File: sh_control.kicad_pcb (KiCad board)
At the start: 4 copper layers, 70 x 70 mm, 121 parts, among them IC1 SN65220DBVT, IC2 TUSB2046IBVF, IC3 ATMEGA328P-AU, IC4 FT232RL-REEL, IC5 LM317MDCY, J1 12401598E4#2A, J2 10129381-906001BLF, J3 10129381-906001BLF, Y1 6Mhz, Y2 16 MHz

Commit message: deleted all, beginning of eval board
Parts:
- removed C1, C14, C18, C19, C20, C21, C22, C23, C6: 10 uF, SamacSys_Parts:CAPC3216X180N
- removed C13: 1 uF, SamacSys_Parts:CAPC3216X210N
- removed C15, C17, C2, C4, C7: 0.1 uF, SamacSys_Parts:CAPC3216X88N
- removed C16, C24, C25, C26, C27: 100 uF, SamacSys_Parts:CAPPRD250W45D630H500
- removed C3, C5: 27 pF, SamacSys_Parts:CAPC3216X170N
- removed D1, D2, D3: FM4002-W, SamacSys_Parts:DIOM5025X231N
- removed DN_1, DN_2, DN_3, DN_4, DP_1, DP_2, DP_3, DP_4, GND1, GND2, GND_1, GND_2, GND_3, GND_4, LED_VCC_in1, LED_VCC_out1, VCC_1, VCC_2, VCC_3, VCC_4: TestPoint, TestPoint:TestPoint_Pad_2.0x2.0mm
- removed F1, F2: Fuse, SamacSys_Parts:FUSC4632X85N
- removed H1, H2, H3, H4: MountingHole, MountingHole:MountingHole_3.2mm_M3
- removed J1: 12401598E4#2A, usb c connector:AMPHENOL_12401598E4#2A
- removed J2, J3: 10129381-906001BLF, SamacSys_Parts:HDRV6W67P254_2X3_762X483X858P
- removed LED4, LED5, LED6, LED7, LED8, LED9: COM-13667, SamacSys_Parts:COM13667
- removed R1, R12, R15, R17, R18, R19, R2, R20, R7, R9: 22, SamacSys_Parts:RESC3116X70N
- removed R10, R13, R16, R21, R22, R23, R5, R8: 15K, SamacSys_Parts:RESC3216X75N
- removed R11, R4: 1K5, SamacSys_Parts:RESC2012X60N
- removed R14, R6: 4K7, SamacSys_Parts:RESC3116X65N
- removed R3: 10K, SamacSys_Parts:RESC3216X60N
- removed R31, R33: 390 R, SamacSys_Parts:RESC3216X60N
- removed R32: 240 R, SamacSys_Parts:RESC3216X75N
- removed Y1: 6Mhz, SamacSys_Parts:LFXTAL036567BULK
- added IC6: TLV76733DGNR, SamacSys_Parts:SOP65P490X110-9N, F.Cu at (90.3, 85.0)
- C10, C11, C12, C28, C29, C30, C31, C32, C33, C34, C35, C8, C9, IC3, IC4, LED1, LED2, LED3, PB0, PC5, PD2, PD3, PD7, R24, R25, R26, R27, R28, R29, R30, Y2: moved to F.Cu
- IC1: value SN65220DBVT -> TLV76733DGNR; footprint SamacSys_Parts:SOT95P280X145-6N -> SamacSys_Parts:SOP65P490X110-9N
- IC5: value LM317MDCY -> TPD2E2U06DCKR; footprint SamacSys_Parts:SOT230P700X180-4N -> SamacSys_Parts:SOT65P210X110-3N
- moved IC1 87.1 mm to (122.9, 58.9)
- moved PC5 86.8 mm to (128.6, 58.6)
- moved PD3 83.1 mm to (132.7, 58.6)
- moved PB0 81.9 mm to (121.3, 63.2)
- moved PD2 80.9 mm to (129.4, 62.6)
- moved PD7 72.7 mm to (125.3, 63.2)
- moved C35 71.8 mm to (112.1, 58.3), turned to 0 degrees
- moved C34 70.3 mm to (112.1, 61.7), turned to 0 degrees
- moved C29 70.2 mm to (106.4, 68.3), turned to 0 degrees
- moved C33 66.1 mm to (106.5, 65.0), turned to 0 degrees
- moved R30 66.0 mm to (106.6, 61.6), turned to 0 degrees
- moved C31 61.6 mm to (99.8, 69.8), turned to 0 degrees
- moved C30 60.3 mm to (99.2, 73.1), turned to 0 degrees
- moved C10 59.4 mm to (111.6, 68.3), turned to 0 degrees
- moved C12 59.2 mm to (111.9, 65.1)
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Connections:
- C10 pad 2: USB_GND -> GND
- C12 pad 1: USB_GND -> GND
- C28 pad 2: USB_GND -> GND
- C29 pad 2: USB_GND -> GND
- C30 pad 2: USB_GND -> GND
- C31 pad 2: USB_GND -> GND
- C32 pad 2: USB_GND -> GND
- C33 pad 2: USB_GND -> GND
- C34 pad 2: USB_GND -> GND
- C35 pad 2: USB_GND -> GND
- C8 pad 1: USB_GND -> GND
- C9 pad 1: USB_GND -> GND
- IC1 pad 2: USB_GND -> Net-(IC1-Pad2)
- IC1 pad 4: DN_hub -> Net-(IC1-Pad4)
- IC1 pad 5: USB_GND -> Net-(IC1-Pad5)
- IC1 pad 6: DP_hub -> Net-(IC1-Pad6)
- IC2 pad 14: Net-(IC2-Pad10) -> Net-(IC2-Pad14)
- IC2 pad 18: Net-(IC2-Pad10) -> Net-(IC2-Pad18)
- IC2 pad 22: Net-(IC2-Pad10) -> Net-(IC2-Pad22)
- IC2 pad 25: +3V3 -> Net-(IC2-Pad25)
- IC2 pad 27: USB_GND -> Net-(IC2-Pad27)
- IC2 pad 28: USB_GND -> Net-(IC2-Pad28)
- IC2 pad 3: +3V3 -> Net-(IC2-Pad3)
- IC2 pad 31: USB_GND -> Net-(IC2-Pad31)
- IC2 pad 6: USB_GND -> Net-(IC2-Pad6)
- IC2 pad 7: USB_GND -> Net-(IC2-Pad7)
- IC2 pad 8: USB_GND -> Net-(IC2-Pad8)
- IC3 pad 21: USB_GND -> GND
- IC3 pad 3: USB_GND -> GND
- IC3 pad 5: USB_GND -> GND
- IC4 pad 18: USB_GND -> GND
- IC4 pad 21: USB_GND -> GND
- IC4 pad 25: USB_GND -> GND
- IC4 pad 26: USB_GND -> GND
- IC4 pad 7: USB_GND -> GND
- IC5 pad 2: +3V3 -> Net-(IC5-Pad2)
- IC5 pad 3: VCC -> GND
- LED1 pad 1: USB_GND -> GND
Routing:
- net USB_GND: track 554.8 -> 0.00 mm, vias 15 -> 0
- net VCC: track 233.7 -> 0.00 mm, vias 11 -> 0
- net LED_control: track 117.9 -> 0.00 mm, vias 2 -> 0
- net DN_FT232RL: track 108.1 -> 0.00 mm, vias 2 -> 0
- net DP_hub: track 96.8 -> 0.00 mm, vias 6 -> 0
- net DN_hub: track 92.1 -> 0.00 mm, vias 6 -> 0
- net +3V3: track 86.1 -> 0.00 mm, vias 4 -> 0
- net DN_2: track 83.3 -> 0.00 mm, vias 4 -> 0
- net Net-(C18-Pad2): track 72.2 -> 0.00 mm, vias 1 -> 0
- net DP_2: track 69.3 -> 0.00 mm, vias 6 -> 0
- net Net-(IC2-Pad19): track 67.2 -> 0.00 mm, vias 2 -> 0
- net DP_FT232RL: track 55.5 -> 0.00 mm, vias 3 -> 0
- net Net-(IC2-Pad11): track 47.0 -> 0.00 mm, vias 2 -> 0
- net Net-(IC2-Pad24): track 44.1 -> 0.00 mm, vias 2 -> 0
- net +5V: track 43.2 -> 0.00 mm
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- removed copper zone on B.Cu, net USB_GND
- removed copper zone on F.Cu, net USB_GND
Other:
- board outline removed
- board text removed: "penholder v3.1 by Maximilian Altrichter"

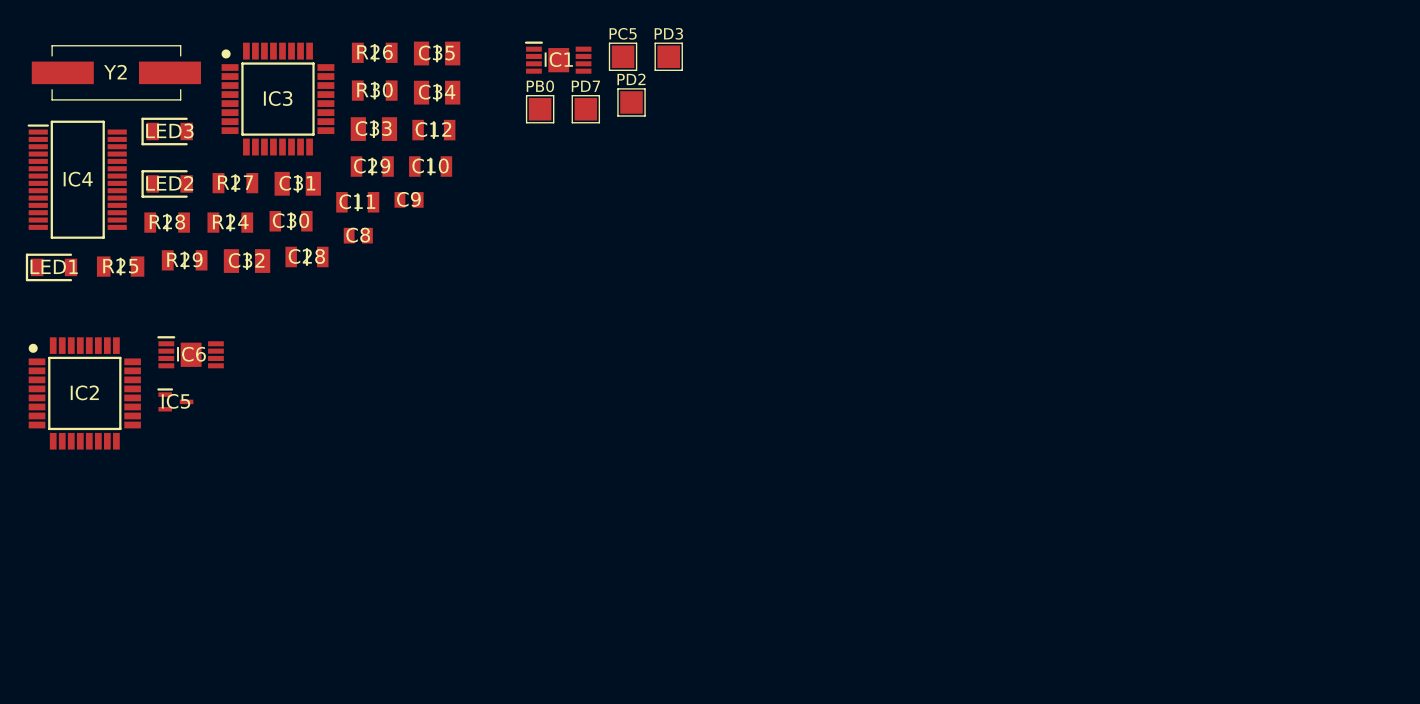
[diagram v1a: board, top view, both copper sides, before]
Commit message: split in two boards from now on
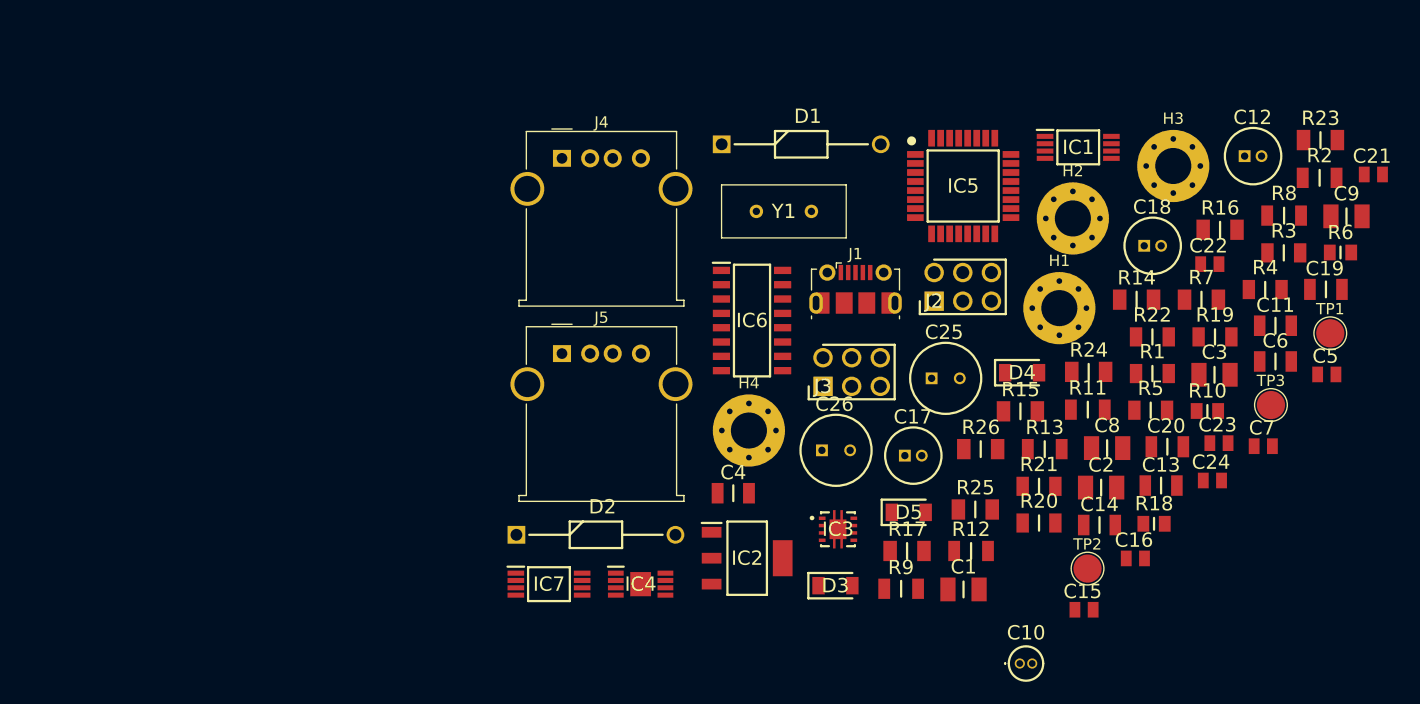
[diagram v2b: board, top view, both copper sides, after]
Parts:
- removed C28, C29, C30: 0,1 uF, SamacSys_Parts:CAPC3216X88N
- removed C31, C32, C33, C34, C35: 1 uF, SamacSys_Parts:CAPC3216X210N
- removed LED1, LED2, LED3: Green, SamacSys_Parts:LEDC3214X78N
- removed PB0, PC5, PD2, PD3, PD7: TestPoint, TestPoint:TestPoint_Pad_2.0x2.0mm
- removed R27: 10 K, SamacSys_Parts:RESC3216X60N
- removed R28, R29, R30: 1 K, SamacSys_Parts:RESC3216X60N
- removed Y2: 16 MHz, SamacSys_Parts:ECS49205PXTR
- added C1: 1uF, storage:C_1uF, F.Cu at (158.8, 105.8)
- added C13: 0.1uF, storage:C_0.1uF, F.Cu at (176.3, 96.6)
- added C14: 0.1uF, storage:C_0.1uF, F.Cu at (170.9, 100.1)
- added C15: 22pF, storage:C_22pF, F.Cu at (169.5, 107.6)
- added C16: 22pF, storage:C_22pF, F.Cu at (174.0, 103.0)
- added C17: 4.7uF, storage:C_4.7uF, F.Cu at (153.6, 93.9)
- added C18: 4.7uF, storage:C_4.7uF, F.Cu at (174.8, 75.3)
- added C19: 27uF, storage:C_27pF, F.Cu at (190.9, 79.2)
- added C2: 1uF, storage:C_1uF, F.Cu at (171.0, 96.8)
- added C20: 27uF, storage:C_27pF, F.Cu at (176.9, 93.1)
- added C21: 22pF, storage:C_22pF, F.Cu at (195.1, 69.0)
- added C22: 22pF, storage:C_22pF, F.Cu at (180.6, 76.9)
- added C23: 22pF, storage:C_22pF, F.Cu at (181.5, 92.8)
- added C24: 22pF, storage:C_22pF, F.Cu at (180.9, 96.1)
- added C25: 100uF, storage:C_100uF, F.Cu at (156.0, 87.1)
- added C26: 100uF, storage:C_100uF, F.Cu at (146.3, 93.5)
- added C3: 1uF, storage:C_1uF, F.Cu at (181.1, 86.8)
- added C4: 10uF, storage:C_10uF, F.Cu at (138.4, 97.3)
- added C5: 22pF, storage:C_22pF, F.Cu at (191.0, 86.7)
- added C6: 0.1uF, storage:C_0.1uF, F.Cu at (186.5, 85.6)
- added C7: 22pF, storage:C_22pF, F.Cu at (185.4, 93.1)
- added D1: 1N4002, storage:D_1N4002, F.Cu at (137.4, 66.3)
- added D2: 1N4002, storage:D_1N4002, F.Cu at (119.2, 100.9)
- added D3: Buck_1, SamacSys_Parts:LEDC3214X78N, F.Cu at (147.5, 105.5)
- added D4: Buck_2, SamacSys_Parts:LEDC3214X78N, F.Cu at (164.0, 86.6)
- added D5: LDO, SamacSys_Parts:LEDC3214X78N, F.Cu at (154.0, 99.0)
- added H1: MountingHole_Pad, MountingHole:MountingHole_3.2mm_M3_Pad_Via, F.Cu at (167.3, 80.8)
- added H2: MountingHole_Pad, MountingHole:MountingHole_3.2mm_M3_Pad_Via, F.Cu at (168.5, 72.9)
- added H3: MountingHole_Pad, MountingHole:MountingHole_3.2mm_M3_Pad_Via, F.Cu at (177.4, 68.2)
- added H4: MountingHole_Pad, MountingHole:MountingHole_3.2mm_M3_Pad_Via, F.Cu at (139.8, 91.7)
- added IC7: SN75240PW, SamacSys_Parts:SOP65P640X120-8N, F.Cu at (122.1, 105.3)
- added J1: USB_B_Micro, Connector_USB:USB_Micro-B_Molex-105017-0001, F.Cu at (149.2, 79.2)
- added J2: 10129381-906001BLF, SamacSys_Parts:HDRV6W67P254_2X3_762X483X858P, F.Cu at (156.2, 80.2)
- added J3: 10129381-906001BLF, SamacSys_Parts:HDRV6W67P254_2X3_762X483X858P, F.Cu at (146.4, 87.8)
- added J4: USB_A, Connector_USB:USB_A_Molex_67643_Horizontal, F.Cu at (123.2, 67.6)
- added J5: USB_A, Connector_USB:USB_A_Molex_67643_Horizontal, F.Cu at (123.2, 84.9)
- added R1: 22, storage:R_22, F.Cu at (175.6, 86.6)
- added R10: 1.5k, storage:R_1K5, F.Cu at (180.4, 90.0)
- added R11: 1k, storage:R_1K, F.Cu at (169.8, 89.8)
- added R12: 1k, storage:R_1K, F.Cu at (159.5, 102.4)
- added R13: 1k, storage:R_1K, F.Cu at (166.0, 93.3)
- added R14: 15k, storage:R_15K, F.Cu at (174.2, 80.1)
- added R15: 15k, storage:R_15K, F.Cu at (163.9, 90.0)
- added R16: 15k, storage:R_15K, F.Cu at (181.6, 73.9)
- added R17: 15k, storage:R_15K, F.Cu at (153.8, 102.4)
- added R18: 1.5k, storage:R_1K5, F.Cu at (175.7, 100.0)
- added R19: 22, storage:R_22, F.Cu at (181.1, 83.4)
- added R2: 390, storage:R_390, F.Cu at (190.4, 69.3)
- added R20: 22, storage:R_22, F.Cu at (165.5, 99.9)
- added R21: 22, storage:R_22, F.Cu at (165.5, 96.6)
- added R22: 22, storage:R_22, F.Cu at (175.6, 83.4)
- added R23: 15k, storage:R_15K, F.Cu at (190.5, 65.9)
- added R3: 22, storage:R_22, F.Cu at (187.2, 75.9)
- added R4: 22, storage:R_22, F.Cu at (185.6, 79.2)
- added R5: 22, storage:R_22, F.Cu at (175.4, 89.9)
- added R6: 1.5k, storage:R_1K5, F.Cu at (192.2, 75.9)
- added R7: 240, storage:R_240, F.Cu at (179.9, 80.1)
- added R8: 390, storage:R_390, F.Cu at (187.2, 72.6)
- added R9: 10k, storage:R_10K, F.Cu at (153.3, 105.7)
- added TP1: GND, TestPoint:TestPoint_Pad_D2.5mm, F.Cu at (191.3, 83.1)
- added TP2: VBUS, TestPoint:TestPoint_Pad_D2.5mm, F.Cu at (169.8, 103.9)
- added TP3: TestPoint, TestPoint:TestPoint_Pad_D2.5mm, F.Cu at (186.1, 89.4)
- added Y1: 6MHz, SamacSys_Parts:LFXTAL036567BULK, F.Cu at (140.4, 72.3)
- C10: value 0.1 uF -> 2.2uF; footprint SamacSys_Parts:CAPC3216X88N -> storage:C_2.2F
- C11: value 0,1 uF -> 0.1uF; footprint SamacSys_Parts:CAPC3216X88N -> storage:C_0.1uF
- C12: value 0.1 uF -> 4.7uF; footprint SamacSys_Parts:CAPC3216X88N -> storage:C_4.7uF
- C8, C9: value 22 pF -> 1uF; footprint SamacSys_Parts:CAPC2012X70N -> storage:C_1uF
- IC1: value TLV76733DGNR -> SN75240PW; footprint SamacSys_Parts:SOP65P490X110-9N -> SamacSys_Parts:SOP65P640X120-8N
- IC2: value TUSB2046IBVF -> LM317MDCY; footprint SamacSys_Parts:QFP80P900X900X160-32N -> SamacSys_Parts:SOT230P700X180-4N
- IC3: value ATMEGA328P-AU -> TPS73533DRBT; footprint SamacSys_Parts:QFP80P900X900X120-32N -> SamacSys_Parts:TPS73533DRBT
- IC4: value FT232RL-REEL -> TLV76733DGNR; footprint SamacSys_Parts:SOP65P778X200-28N -> SamacSys_Parts:SOP65P490X110-9N
- IC5: value TPD2E2U06DCKR -> TUSB2046IBVF; footprint SamacSys_Parts:SOT65P210X110-3N -> SamacSys_Parts:QFP80P900X900X160-32N
- IC6: value TLV76733DGNR -> TPS2044BDR; footprint SamacSys_Parts:SOP65P490X110-9N -> SamacSys_Parts:SOIC127P600X175-16N
- R24, R26: value 1 K -> 15k; footprint SamacSys_Parts:RESC3216X60N -> storage:R_15K
- R25: value 240 R -> 15k; footprint SamacSys_Parts:RESC3216X75N -> storage:R_15K
- moved C9 83.1 mm to (192.8, 72.7)
- moved C11 82.1 mm to (186.5, 82.4)
- moved R25 78.8 mm to (159.9, 98.7)
- moved R24 77.2 mm to (169.9, 86.5)
- moved IC5 72.4 mm to (158.8, 70.0)
- moved C12 71.9 mm to (183.7, 67.4)
- moved C8 69.0 mm to (171.5, 93.3)
- moved C10 68.8 mm to (164.3, 112.3)
- moved R26 64.2 mm to (160.3, 93.3)
- moved IC3 62.6 mm to (147.7, 100.5)
- moved IC4 61.4 mm to (130.2, 105.3)
- moved IC2 60.5 mm to (139.6, 103.0)
- moved IC6 49.8 mm to (140.1, 81.9)
- moved IC1 46.7 mm to (169.0, 66.6)
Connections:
- C10 pad 1: VCC -> 3V3_Buck_1
- C11 pad 1: Net-(C11-Pad1) -> VBUS
- C11 pad 2: Net-(C11-Pad2) -> GND
- C12 pad 1: GND -> VBUS
- C12 pad 2: VCC -> GND
- C8 pad 1: GND -> 3V3_LDO
- C8 pad 2: Net-(C8-Pad2) -> GND
- C9 pad 1: GND -> Net-(C9-Pad1)
- C9 pad 2: Net-(C9-Pad2) -> GND
- IC1 pad 1: Net-(IC1-Pad1) -> GND
- IC1 pad 3: Net-(IC1-Pad3) -> GND
- IC1 pad 5: Net-(IC1-Pad5) -> GND
- IC1 pad 7: Net-(IC1-Pad7) -> GND
- IC2 pad 2: Net-(IC2-Pad2) -> 3V3_Buck_2
- IC2 pad 3: Net-(IC2-Pad3) -> Buck_2
- IC3 pad 1: /atmega328P/PD3 -> 3V3_LDO
- IC3 pad 3: GND -> Net-(C9-Pad1)
- IC3 pad 4: VCC -> GND
- IC3 pad 5: GND -> Net-(IC3-Pad5)
- IC3 pad 6: VCC -> Net-(IC3-Pad6)
- IC3 pad 7: Net-(C8-Pad2) -> Net-(IC3-Pad7)
- IC3 pad 8: Net-(C9-Pad2) -> LDO
- IC3 pad 9: Net-(IC3-Pad9) -> GND
- IC4 pad 1: Net-(IC4-Pad1) -> 3V3_Buck_1
- IC4 pad 2: Net-(C11-Pad1) -> 3V3_Buck_1
- IC4 pad 4: VCC -> GND
- IC4 pad 6: Net-(IC4-Pad6) -> GND
- IC4 pad 7: GND -> Net-(IC4-Pad7)
- IC4 pad 8: Net-(IC4-Pad8) -> Buck_1
- IC4 pad 9: Net-(IC4-Pad9) -> GND
- IC5 pad 1: Net-(IC5-Pad1) -> DP0
- IC5 pad 2: Net-(IC5-Pad2) -> DMO
- IC5 pad 3: GND -> VCC
- IC6 pad 1: Net-(C4-Pad1) -> GND
- IC6 pad 2: Net-(C4-Pad1) -> VBUS
- IC6 pad 3: Net-(IC6-Pad3) -> PWRON1
- IC6 pad 4: GND -> PWRON2
- IC6 pad 5: Net-(IC6-Pad5) -> GND
- IC6 pad 6: GND -> VBUS
- IC6 pad 7: Net-(IC6-Pad7) -> PWRON3
- IC6 pad 8: VBUS -> PWRON4
- IC6 pad 9: Net-(IC6-Pad9) -> OVRCUR4
- R24 pad 1: Net-(IC4-Pad5) -> GND
- R24 pad 2: Net-(IC3-Pad31) -> DP_downstream2
- R25 pad 1: LED_control -> GND
- R25 pad 2: Net-(IC3-Pad10) -> DM_downstream1
- R26 pad 1: Net-(IC4-Pad1) -> GND
- R26 pad 2: Net-(IC3-Pad30) -> DM_downstream2

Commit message: finished schematic, placing parts and so on
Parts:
- removed D4: Buck_2, SamacSys_Parts:LEDC3214X78N
- removed D5: LDO, SamacSys_Parts:LEDC3214X78N
- removed J4, J5: USB_A, Connector_USB:USB_A_Molex_67643_Horizontal
- removed TP1: GND, TestPoint:TestPoint_Pad_D2.5mm
- removed TP2: VBUS, TestPoint:TestPoint_Pad_D2.5mm
- added Buck_2: Buck_2, SamacSys_Parts:LEDC3214X78N, F.Cu at (157.1, 36.7)
- added C27: 22pF, storage:C_22pF, F.Cu at (159.5, 77.3)
- added C28: 22pF, storage:C_22pF, F.Cu at (150.9, 77.3)
- added C29: 22pF, storage:C_22pF, F.Cu at (157.7, 77.3)
- added C30: 22pF, storage:C_22pF, F.Cu at (149.1, 77.3)
- added C31: 100uF, storage:C_100uF, F.Cu at (188.7, 95.5)
- added C32: 100uF, storage:C_100uF, F.Cu at (188.7, 80.0)
- added G***: LOGO, logo_hub:logo, F.Cu at (139.4, 117.9)
- added GND1: GND, TestPoint:TestPoint_Pad_D2.5mm, F.Cu at (162.6, 124.5)
- added LDO1: LDO, SamacSys_Parts:LEDC3214X78N, F.Cu at (180.8, 36.7)
- added PortA1: USB_A, Connector_USB:USB_A_Molex_67643_Horizontal, F.Cu at (121.2, 104.6)
- added PortB1: USB_A, Connector_USB:USB_A_Molex_67643_Horizontal, F.Cu at (121.2, 65.5)
- added PortC1: USB_A, Connector_USB:USB_A_Molex_67643_Horizontal, F.Cu at (188.7, 111.8)
- added PortD1: USB_A, Connector_USB:USB_A_Molex_67643_Horizontal, F.Cu at (188.7, 72.9)
- added R27: 15k, storage:R_15K, F.Cu at (182.9, 104.6)
- added R28: 15k, storage:R_15K, F.Cu at (183.1, 66.0)
- added R29: 15k, storage:R_15K, F.Cu at (182.9, 111.7)
- added R30: 15k, storage:R_15K, F.Cu at (183.1, 72.6)
- added VBUS1: VBUS, TestPoint:TestPoint_Pad_D2.5mm, F.Cu at (147.3, 124.5)
- R14, R15, R16, R17: value 15k -> 22; footprint storage:R_15K -> storage:R_22
- moved R23 78.9 mm to (127.0, 112.8), turned to 270 degrees
- moved C10 72.6 mm to (126.7, 50.2), turned to 270 degrees
- moved Buck_1 70.2 mm to (133.3, 36.7)
- moved H2 62.2 mm to (116.8, 38.3)
- moved TP3 61.4 mm to (134.6, 56.0)
- moved R12 61.3 mm to (157.3, 41.1)
- moved R11 60.7 mm to (133.5, 41.1)
- moved C1 60.2 mm to (181.9, 50.2)
- moved C2 57.8 mm to (137.6, 49.6), turned to 270 degrees
- moved IC3 56.5 mm to (176.7, 52.0)
- moved IC4 55.4 mm to (132.4, 50.0)
- moved R13 54.3 mm to (181.0, 41.1)
- moved R5 54.1 mm to (147.5, 43.5), turned to 90 degrees
- moved IC2 54.1 mm to (156.1, 51.5)
- moved D2 53.9 mm to (152.9, 58.8)
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- renumbered D3 to Buck_1
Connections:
- IC1 pad 6: Net-(IC1-Pad6) -> (no net)
- IC1 pad 8: Net-(IC1-Pad8) -> (no net)
- IC3 pad 2: Net-(IC3-Pad2) -> (no net)
- IC3 pad 6: Net-(IC3-Pad6) -> (no net)
- IC3 pad 7: Net-(IC3-Pad7) -> (no net)
- IC4 pad 3: Net-(IC4-Pad3) -> (no net)
- IC4 pad 7: Net-(IC4-Pad7) -> (no net)
- IC5 pad 32: Net-(IC5-Pad32) -> (no net)
- IC5 pad 5: Net-(IC5-Pad5) -> (no net)
- IC6 pad 10: Net-(IC6-Pad10) -> OUT4
- IC6 pad 11: Net-(IC6-Pad11) -> OUT3
- J1 pad 4: Net-(J1-Pad4) -> (no net)
- R14 pad 1: GND -> DM_downstream3
- R14 pad 2: DP3 -> DM3
- R15 pad 1: GND -> DP_downstream3
- R15 pad 2: DM3 -> DP3
- R16 pad 1: GND -> DM_downstream4
- R17 pad 1: GND -> DP_downstream4
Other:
- board outline added: 86.4 x 94.7 mm
- board text added: "3V3_1 3V3_2 LDO"
- board text added: "B1 B2 LDO"
- board text added: "USB HUB by Maximilian Altrichter"
